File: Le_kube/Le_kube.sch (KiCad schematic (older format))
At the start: 1 part

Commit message: screen done
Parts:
- removed U?: ATmega328P-AU, Package_QFP:TQFP-32_7x7mm_P0.8mm, symbol MCU_Microchip_ATmega:ATmega328P-AU
- added U?: ATmega328PB-AU, Package_QFP:TQFP-32_7x7mm_P0.8mm, symbol MCU_Microchip_ATmega:ATmega328PB-AU
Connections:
- wire segments 2 -> 15
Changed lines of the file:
@@
 $Descr A4 11693 8268
 encoding utf-8
-Sheet 1 2
+Sheet 1 3
 Title ""
 Date ""
@@
 Comment4 ""
 $EndDescr
-$Comp
-L MCU_Microchip_ATmega:ATmega328P-AU U?
-U 1 1 606383C9
-P 3000 2750
-F 0 "U?" H 3000 1161 50  0000 C CNN
-F 1 "ATmega328P-AU" H 3000 1070 50  0000 C CNN
-F 2 "Package_QFP:TQFP-32_7x7mm_P0.8mm" H 3000 2750 50  0001 C CIN
-F 3 "http://ww1.microchip.com/downloads/en/DeviceDoc/ATmega328_P%20AVR%20MCU%20with%20picoPower%20Technology%20Data%20Sheet%2040001984A.pdf" H 3000 2750 50  0001 C CNN
-	1    3000 2750
-	1    0    0    -1
-$EndComp
-Wire Wire Line
-	3600 1850 5150 1850
-Wire Wire Line
-	3600 1950 5150 1950
-$Sheet
-S 7650 3550 950  850
-U 60669017
-F0 "Sheet60669016" 50
-F1 "ssd1306_128_64.sch" 50
-$EndSheet
 $Sheet
 S 7900 2350 900  850
@@
 F1 "Temp_Sensor.sch" 50
 $EndSheet
+$Sheet
+S 6800 3150 950  850
+U 60669017
+F0 "Sheet60669016" 50
+F1 "ssd1306_128_64.sch" 50
+F2 "CS" I L 6800 3250 50
+F3 "DC" I L 6800 3350 50
+F4 "RES" I L 6800 3450 50
+F5 "SDA_D1" I L 6800 3550 50
+F6 "SCK_D0" I L 6800 3650 50
+$EndSheet
+Wire Wire Line
+	3600 1650 6050 1650
+Wire Wire Line
+	6050 1650 6050 3450
+Wire Wire Line
+	6050 3450 6800 3450
+Wire Wire Line
+	3600 3950 6250 3950
+Wire Wire Line
+	6250 3950 6250 3250
+Wire Wire Line
+	6250 3250 6800 3250
+Wire Wire Line
+	3600 3850 6350 3850
+Wire Wire Line
+	6350 3850 6350 3350
+Wire Wire Line
+	6350 3350 6800 3350
+Wire Wire Line
+	5900 1850 5900 3550
+Wire Wire Line
+	5900 3550 6800 3550
+Wire Wire Line
+	3600 1850 5900 1850
+Wire Wire Line
+	3600 2050 5750 2050
+Wire Wire Line
+	5750 2050 5750 3650
+Wire Wire Line
+	5750 3650 6800 3650
+$Comp
+L MCU_Microchip_ATmega:ATmega328PB-AU U?
+U 1 1 6081701B
+P 3000 2850
+F 0 "U?" H 3000 1261 50  0000 C CNN
+F 1 "ATmega328PB-AU" H 3000 1170 50  0000 C CNN
+F 2 "Package_QFP:TQFP-32_7x7mm_P0.8mm" H 3000 2850 50  0001 C CIN
+F 3 "http://ww1.microchip.com/downloads/en/DeviceDoc/40001906C.pdf" H 3000 2850 50  0001 C CNN
+	1    3000 2850
+	1    0    0    -1
+$EndComp
 $EndSCHEMATC

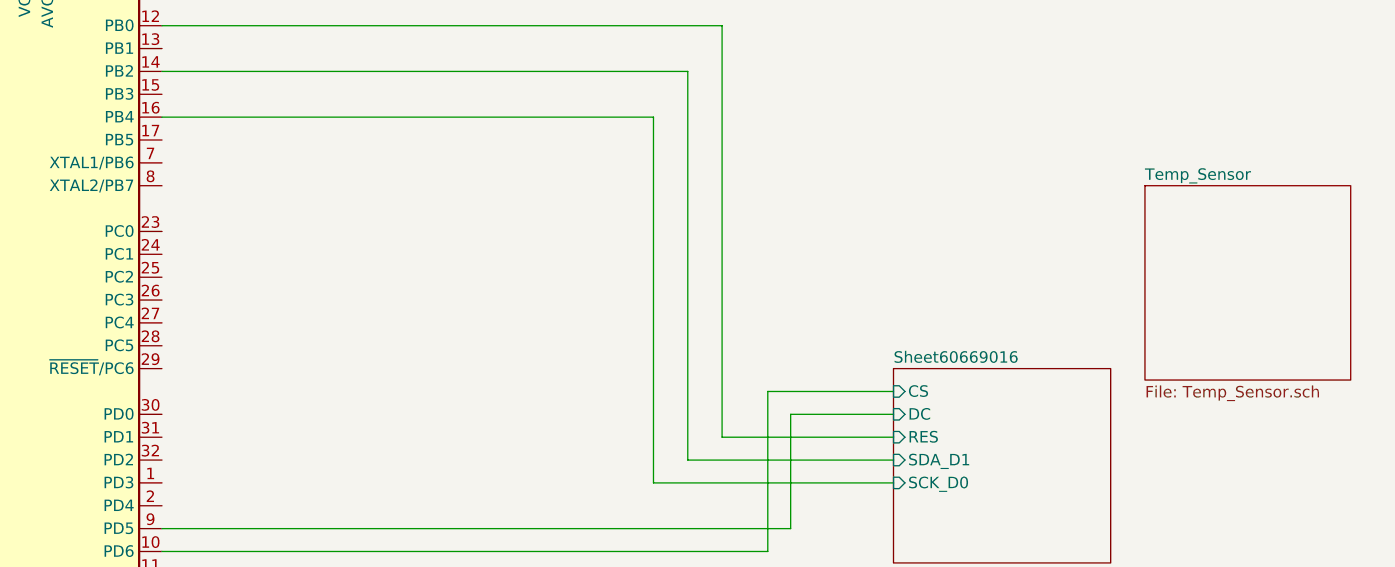
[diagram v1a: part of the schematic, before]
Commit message: merge screen + temp sensor CAO
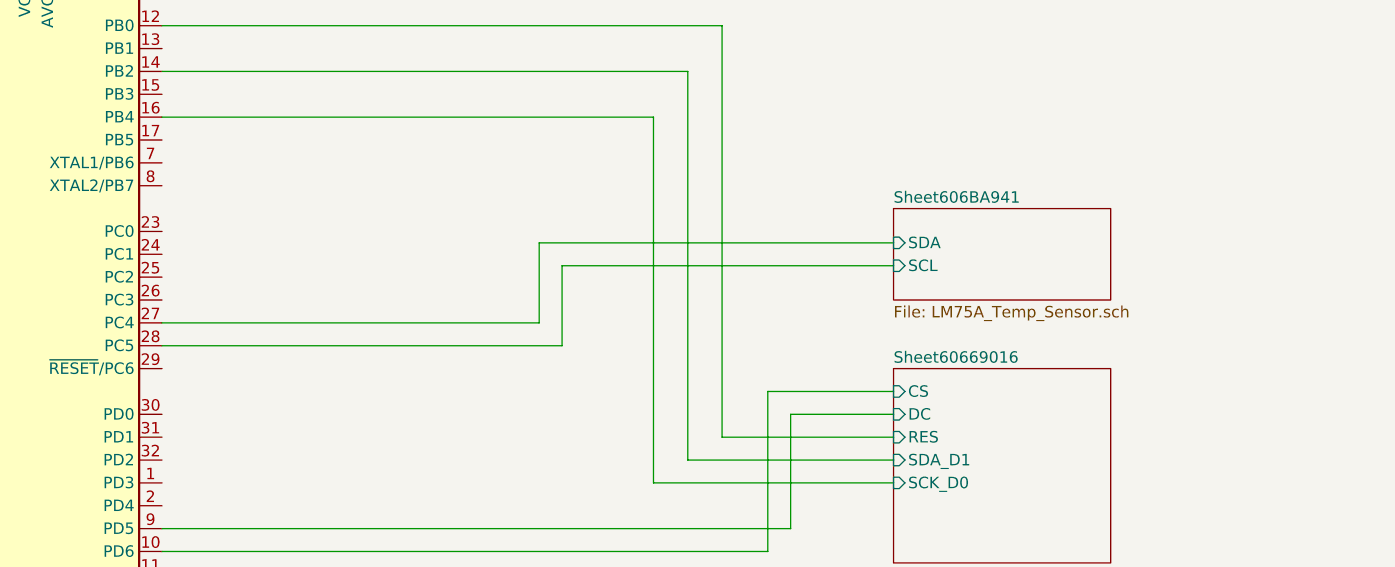
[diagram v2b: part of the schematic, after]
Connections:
- net Sheet606BA941/SDA: now reaches U?.27 (PC4)
- net Sheet606BA941/SCL: now reaches U?.28 (PC5)
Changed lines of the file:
@@
 $EndDescr
 $Sheet
-S 7900 2350 900  850
-U 606B8EB7
-F0 "Temp_Sensor" 50
-F1 "Temp_Sensor.sch" 50
+S 6800 2450 950  400
+U 606BA942
+F0 "Sheet606BA941" 50
+F1 "LM75A_Temp_Sensor.sch" 50
+F2 "SDA" I L 6800 2600 50
+F3 "SCL" I L 6800 2700 50
 $EndSheet
 $Sheet
@@
 	1    0    0    -1
 $EndComp
+Wire Wire Line
+	3600 2950 5250 2950
+Wire Wire Line
+	5250 2950 5250 2600
+Wire Wire Line
+	5250 2600 6800 2600
+Wire Wire Line
+	3600 3050 5350 3050
+Wire Wire Line
+	5350 3050 5350 2700
+Wire Wire Line
+	5350 2700 6800 2700
 $EndSCHEMATC

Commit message: cao
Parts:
- added R?: LDR, symbol Kube_library:LDR
- added R?: 10K, symbol Device:R_Small
- added R? (x4): R_Small, symbol Device:R_Small
- added SW? (x4): SW_Push, symbol Switch:SW_Push
- added U?: ESP8266-01_ESP-01, XCVR_ESP8266-01/ESP-01, symbol ESP01S:ESP8266-01_ESP-01
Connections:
- net Sheet60669016/CS: now also U?.11 (PD7); no longer U?.10 (PD6)
- net Sheet60669016/DC: now also U?.10 (PD6); no longer U?.9 (PD5)
- net Sheet60669016/SCK_D0: now also U?.17 (PB5); no longer U?.16 (PB4)
- net Sheet60669016/SDA_D1: now also U?.15 (PB3); no longer U?.14 (PB2)
- net at U?.1 (PD3): now also R?.2, SW?.1
- net at U?.2 (PD4): now also R?.2, SW?.1
- net at U?.26 (PC3): now also R?.2, R?.~
- net at U?.29 (~RESET~/PC6): now also R?.2, SW?.1
- net at U?.30 (PD0): now also U?.5 (TXD)
- net at U?.31 (PD1): now also U?.1 (RXD)
- new net: R?.2, SW?.1, U?.9 (PD5)
- new net +3V3: R?.1, R?.~, SW?.2, SW?.2, SW?.2, U?.6 (CH_PD), U?.8 (VCC)
- new net GND: R?.1, R?.1, R?.1, R?.1, SW?.2, U?.4 (GND)
- no-connect marks 0 -> 3
